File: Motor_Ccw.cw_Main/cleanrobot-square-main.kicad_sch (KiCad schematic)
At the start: 0 parts

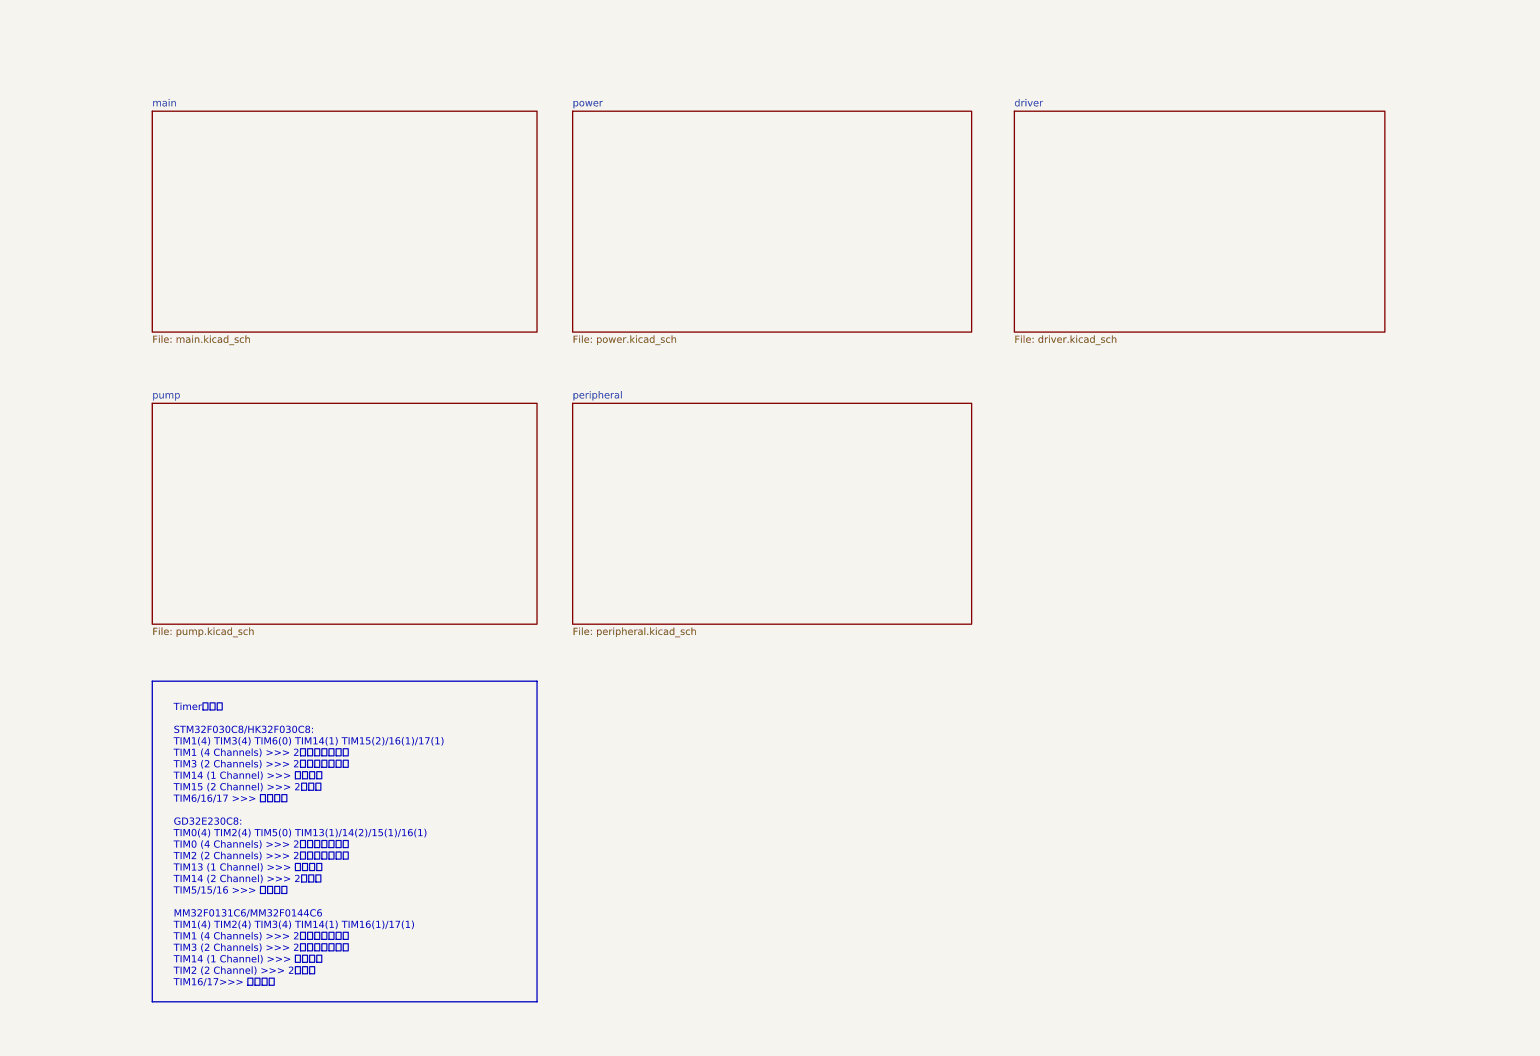
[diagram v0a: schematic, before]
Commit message: 修改电机PWM工程文件
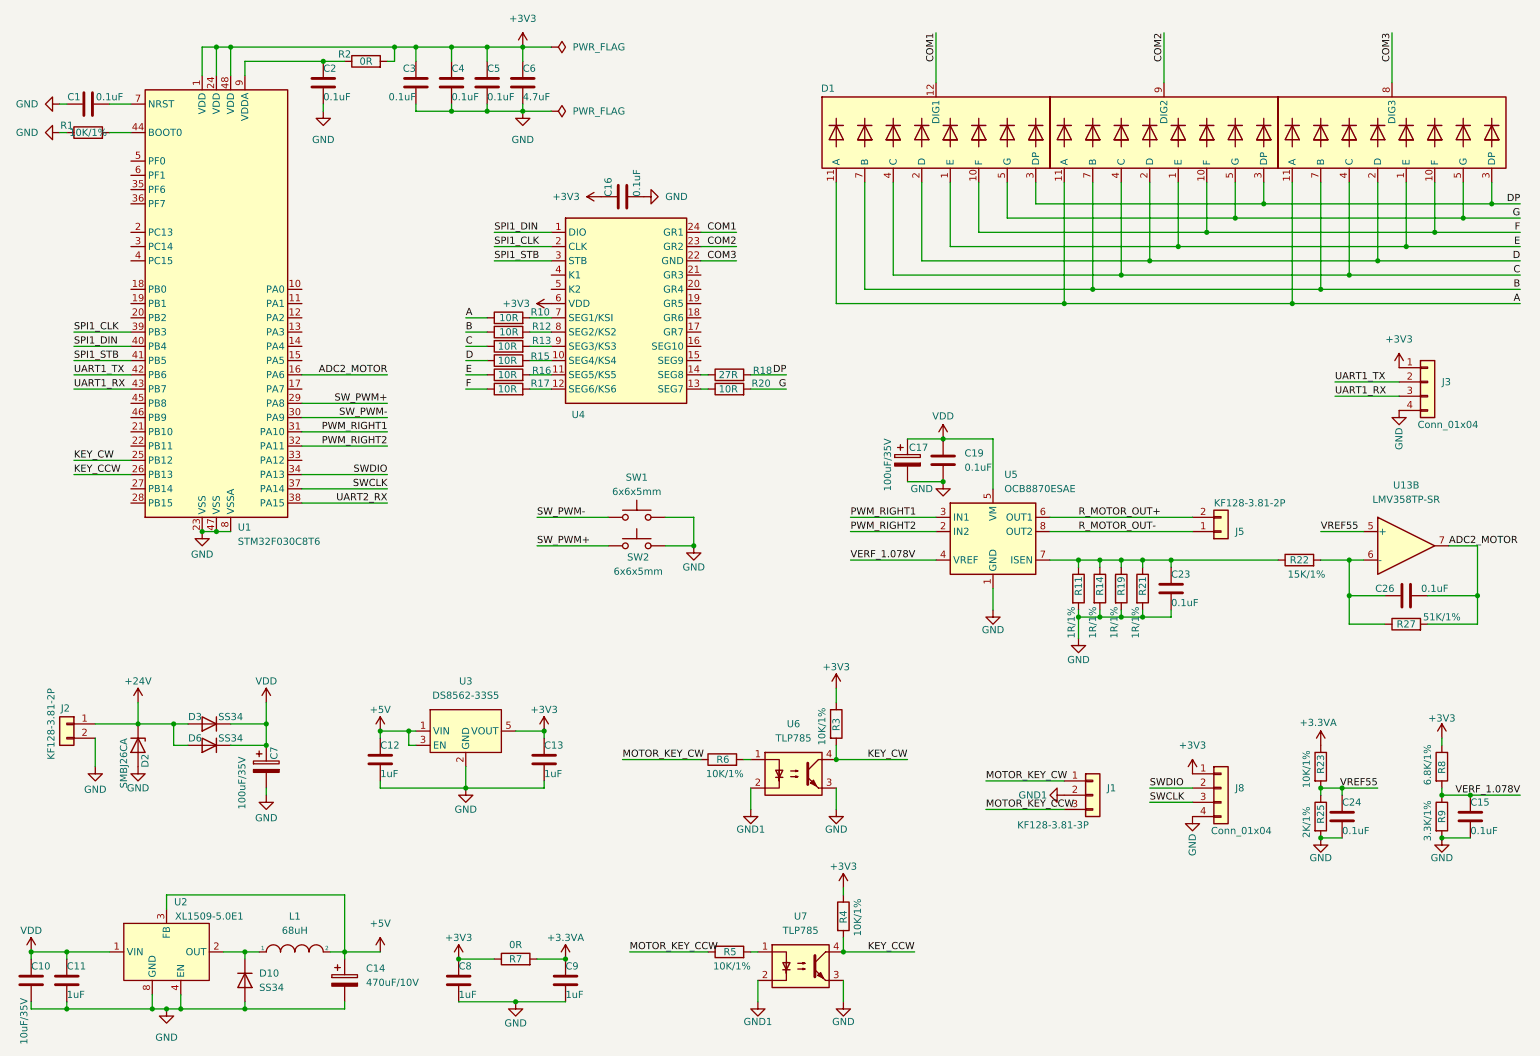
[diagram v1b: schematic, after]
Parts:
- added C1, C15, C16, C19, C2, C23, C24, C26, C3, C4, C5: 0.1uF, Capacitor_SMD:C_0603_1608Metric, symbol Device:C
- added C10: 10uF/35V, Capacitor_SMD:C_0805_2012Metric, symbol Device:C
- added C11, C12, C13, C8, C9: 1uF, Capacitor_SMD:C_0603_1608Metric, symbol Device:C
- added C14: 470uF/10V, Capacitor_THT:CP_Radial_D6.3mm_P2.50mm, symbol Device:C_Polarized
- added C17, C7: 100uF/35V, Capacitor_THT:CP_Radial_D6.3mm_P2.50mm, symbol Device:C_Polarized
- added C6: 4.7uF, Capacitor_SMD:C_0603_1608Metric, symbol Device:C
- added D1: ~, Ovo_SegLed:LED_3x0.56, symbol Ovo_SegLed:LED_3x0.56
- added D10, D3, D6: SS34, Diode_SMD:D_SMA, symbol Device:D
- added D2: SMBJ26CA, Diode_SMD:D_SMB, symbol Device:D_Zener
- added J1: KF128-3.81-3P, TerminalBlock_MetzConnect:TerminalBlock_MetzConnect_Type086_RT03403HBLC_1x03_P3.81mm_Horizontal, symbol Connector_Generic:Conn_01x03
- added J2, J5: KF128-3.81-2P, TerminalBlock_MetzConnect:TerminalBlock_MetzConnect_Type086_RT03402HBLC_1x02_P3.81mm_Horizontal, symbol Connector_Generic:Conn_01x02
- added J3, J8: Conn_01x04, Connector_PinHeader_2.54mm:PinHeader_1x04_P2.54mm_Vertical, symbol Connector_Generic:Conn_01x04
- added L1: 68uH, Ovo_Inductor_SMD:L_GZJ_WNR8045, symbol pspice:INDUCTOR
- added R1, R23, R3, R4, R5, R6: 10K/1%, Resistor_SMD:R_0603_1608Metric, symbol Device:R
- added R10, R12, R13, R15, R16, R17, R20: 10R, Resistor_SMD:R_0805_2012Metric, symbol Device:R
- added R11, R14, R19, R21: 1R/1%, Resistor_SMD:R_0805_2012Metric, symbol Device:R
- added R18: 27R, Resistor_SMD:R_0805_2012Metric, symbol Device:R
- added R2, R7: 0R, Resistor_SMD:R_0603_1608Metric, symbol Device:R
- added R22: 15K/1%, Resistor_SMD:R_0603_1608Metric, symbol Device:R
- added R25: 2K/1%, Resistor_SMD:R_0603_1608Metric, symbol Device:R
- added R27: 51K/1%, Resistor_SMD:R_0603_1608Metric, symbol Device:R
- added R8: 6.8K/1%, Resistor_SMD:R_0603_1608Metric, symbol Device:R
- added R9: 3.3K/1%, Resistor_SMD:R_0603_1608Metric, symbol Device:R
- added SW1, SW2: 6x6x5mm, Ovo_Button_Switch_SMD:SW_Push_1P1T_NO_6x6mm_H5.0mm, symbol Switch:SW_Push
- added U1: STM32F030C8T6, Package_QFP:LQFP-48_7x7mm_P0.5mm, symbol MCU_ST_STM32F0:STM32F030C8Tx
- added U13: LMV358TP-SR, Package_SO:SOIC-8_3.9x4.9mm_P1.27mm, symbol Amplifier_Operational:MCP6002-xSN
- added U2: XL1509-5.0E1, Package_SO:SOIC-8_3.9x4.9mm_P1.27mm, symbol Ovo_Power_Management:XL1509-xxE1
- added U3: DS8562-33S5, Package_TO_SOT_SMD:SOT-23-5, symbol Ovo_Power_Management:RT9013-xx
- added U4: ~, Package_SO:SSOP-24_5.3x8.2mm_P0.65mm, symbol Ovo_Led_TM_16:TM1688
- added U5: OCB8870ESAE, Package_SO:Texas_HTSOP-8-1EP_3.9x4.9mm_P1.27mm_EP2.95x4.9mm_Mask2.4x3.1mm_ThermalVias, symbol Driver_Motor:DRV8870DDA
- added U6, U7: TLP785, Package_DIP:DIP-4_W7.62mm, symbol Isolator:TLP785
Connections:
- new net: C26.1, R22.2, R27.1, U13.6 (-)
- new net: C1.2, U1.7 (NRST)
- new net: R18.1, U4.14 (SEG8)
- new net: R1.2, U1.44 (BOOT0)
- new net: C2.2, R2.1, U1.9 (VDDA)
- new net: C23.1, R11.1, R14.1, R19.1, R21.1, R22.1, U5.7 (ISEN)
- new net: R6.2, U6.1
- new net: R20.1, U4.13 (SEG7)
- new net: R17.2, U4.12 (SEG6/KS6)
- new net: D10.1 (K), L1.1, U2.2 (OUT)
- new net: R5.2, U7.1
- new net: R15.2, U4.10 (SEG4/KS4)
- new net: R16.2, U4.11 (SEG5/KS5)
- new net: R10.2, U4.7 (SEG1/KSI)
- new net: R12.2, U4.8 (SEG2/KS2)
- new net: R13.2, U4.9 (SEG3/KS3)
- new net +24V: D2.1 (K), D3.2 (A), D6.2 (A), J2.1 (Pin_1)
- new net +3.3VA: C9.1, R23.1, R7.2
- new net +3V3: C13.1, C16.1, C3.2, C4.2, C5.2, C6.2, C8.1, J3.1 (Pin_1), J8.1 (Pin_1), R2.2, R3.1, R4.1, R7.1, R8.1, U1.1 (VDD), U1.24 (VDD), U1.48 (VDD), U3.5 (VOUT), U4.6 (VDD)
- new net +5V: C12.1, C14.1, L1.2, U2.3 (FB), U3.1 (VIN), U3.3 (EN)
- new net A: D1.11 (A), R10.1
- new net ADC2_MOTOR: C26.2, R27.2, U1.16 (PA6), U13.7
- new net B: D1.7 (B), R12.1
- new net C: D1.4 (C), R13.1
- new net COM1: D1.12 (DIG1), U4.24 (GR1)
- new net COM2: D1.9 (DIG2), U4.23 (GR2)
- new net COM3: D1.8 (DIG3), U4.22 (GND)
- new net D: D1.2 (D), R15.1
- new net DP: D1.3 (DP), R18.2
- new net E: D1.1 (E), R16.1
- new net F: D1.10 (F), R17.1
- new net G: D1.5 (G), R20.2
- new net GND: C1.1, C10.2, C11.2, C12.2, C13.2, C14.2, C15.2, C16.2, C17.2, C19.2, C2.1, C23.2, C24.2, C3.1, C4.1, C5.1, C6.1, C7.2, C8.2, C9.2, D10.2 (A), D2.2 (A), J2.2 (Pin_2), J3.4 (Pin_4), J8.4 (Pin_4), R1.1, R11.2, R14.2, R19.2, R21.2, R25.2, R9.2, SW1.2, SW2.2, U1.23 (VSS), U1.47 (VSS), U1.8 (VSSA), U2.4 (EN), U2.5 (GND), U2.6 (GND), U2.7 (GND), U2.8 (GND), U3.2 (GND), U5.1 (GND), U5.9 (GND), U6.3, U7.3
- new net GND1: J1.2 (Pin_2), U6.2, U7.2
- new net KEY_CCW: R4.2, U1.26 (PB13), U7.4
- new net KEY_CW: R3.2, U1.25 (PB12), U6.4
- new net MOTOR_KEY_CCW: J1.3 (Pin_3), R5.1
- new net MOTOR_KEY_CW: J1.1 (Pin_1), R6.1
- new net PWM_RIGHT1: U1.31 (PA10), U5.3 (IN1)
- new net PWM_RIGHT2: U1.32 (PA11), U5.2 (IN2)
- new net R_MOTOR_OUT+: J5.2 (Pin_2), U5.6 (OUT1)
- new net R_MOTOR_OUT-: J5.1 (Pin_1), U5.8 (OUT2)
- new net SPI1_CLK: U1.39 (PB3), U4.2 (CLK)
- new net SPI1_DIN: U1.40 (PB4), U4.1 (DIO)
- new net SPI1_STB: U1.41 (PB5), U4.3 (STB)
- new net SWCLK: J8.3 (Pin_3), U1.37 (PA14)
- new net SWDIO: J8.2 (Pin_2), U1.34 (PA13)
- new net SW_PWM+: SW2.1, U1.29 (PA8)
- new net SW_PWM-: SW1.1, U1.30 (PA9)
- new net UART1_RX: J3.3 (Pin_3), U1.43 (PB7)
- new net UART1_TX: J3.2 (Pin_2), U1.42 (PB6)
- new net UART2_RX: U1.38 (PA15)
- new net VDD: C10.1, C11.1, C17.1, C19.1, C7.1, D3.1 (K), D6.1 (K), U2.1 (VIN), U5.5 (VM)
- new net VERF_1.078V: C15.1, R8.2, R9.1, U5.4 (VREF)
- new net VREF55: C24.1, R23.2, R25.1, U13.5 (+)
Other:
- removed sheet driver
- removed sheet main
- removed sheet peripheral
- removed sheet power
- removed sheet pump
- note removed: "Timer分配： STM32F030C8/HK32F030C8: TIM1(4) TIM3(4) TIM6(0) TIM14(1) TIM15(2)/16(1)/17(1) TIM1 (4 Channels) >>> 2个边轮马达驱动 TIM3 (2 Channels) >>> 2个边轮马达测速 TIM14 (1 Channel) >>> 风机马达 TIM15 (2 Channel) >>> 2路喷水 TIM6/16/17 >>> 定时中断 GD32E230C8: TIM0(4) TIM2(4) TIM5(0) TIM13(1)/14(2)/15(1)/16(1) TIM0 (4 Channels) >>> 2个边轮马达驱动 TIM2 (2 Channels) >>> 2个边轮马达测速 TIM13 (1 Channel) >>> 风机马达 TIM14 (2 Channel) >>> 2路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"
